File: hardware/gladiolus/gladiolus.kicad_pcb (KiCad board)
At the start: 4 copper layers, 70.7 x 53.3 mm, 94 parts, among them J1 NEIGHBOR1, J2 NEIGHBOR2, J7 BONUS_ROW, Q1 Q_NPN_BEC, U1 THS4520RGT, U2 AD8330ARQZ, U3 AD9283

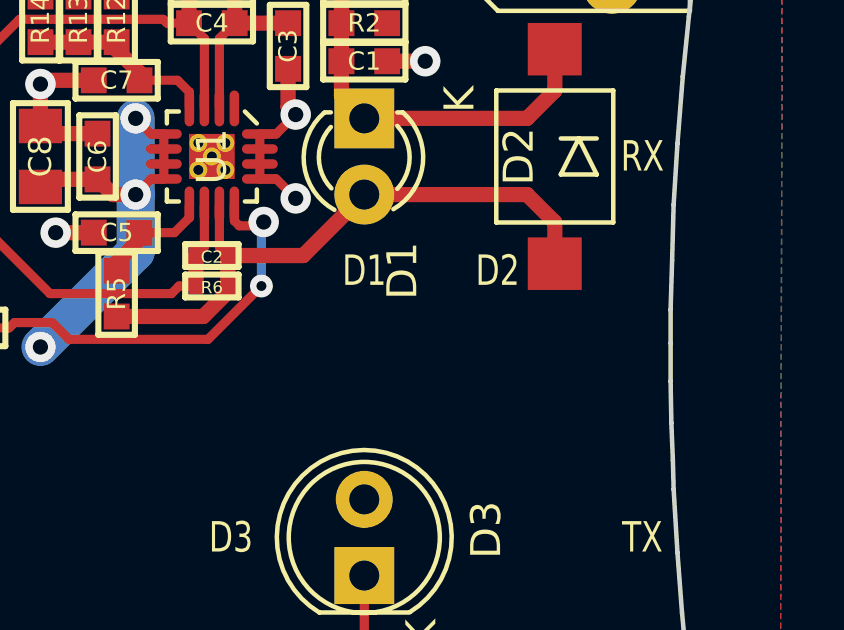
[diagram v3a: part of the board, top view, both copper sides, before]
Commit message: Gladiolus: added female header to block direct TX to RX light
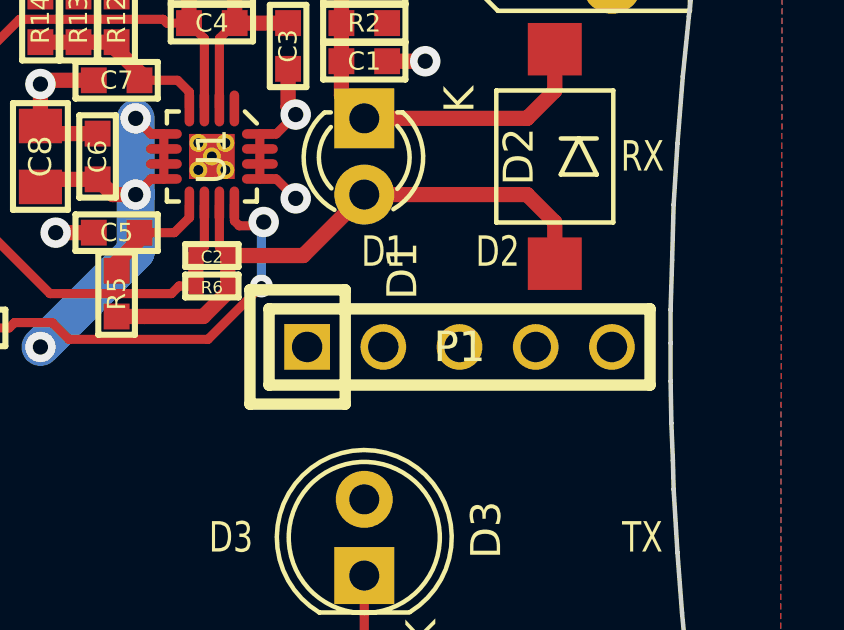
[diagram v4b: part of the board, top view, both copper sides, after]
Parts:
- added P1: CONN_01X05, gsg-modules:HEADER-1x5, F.Cu at (170.8, 95.2)
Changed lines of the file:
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@@
 (kicad_pcb (version 4) (host pcbnew 4.0.4-stable)
   (general
-    (links 228)
+    (links 233)
     (no_connects 0)
     (area 109.525999 68.504999 180.415001 121.995001)
@@
     (tracks 538)
     (zones 0)
-    (modules 94)
+    (modules 95)
     (nets 143)
   )
@@
       (net 132 "Net-(R33-Pad2)"))
   )
+  (module gsg-modules:HEADER-1x5 (layer F.Cu)
+    (at 170.815 95.25)
+    (tags CONN)
+    (fp_text reference P1 (at 0 0) (layer F.SilkS)
+      (effects (font (size 1.016 1.016) (thickness 0.2032)))
+    )
+    (fp_text value CONN_01X05 (at 0 0) (layer F.SilkS) hide
+      (effects (font (size 1.016 1.016) (thickness 0.2032)))
+    )
+    (fp_line (start -6.35 -1.27) (end 6.35 -1.27) (layer F.SilkS) (width 0.381))
+    (fp_line (start 6.35 -1.27) (end 6.35 1.27) (layer F.SilkS) (width 0.381))
+    (fp_line (start 6.35 1.27) (end -6.35 1.27) (layer F.SilkS) (width 0.381))
+    (fp_line (start -3.81 1.905) (end -3.81 -1.905) (layer F.SilkS) (width 0.381))
+    (fp_line (start -3.81 -1.905) (end -6.985 -1.905) (layer F.SilkS) (width 0.381))
+    (fp_line (start -6.985 -1.905) (end -6.985 1.905) (layer F.SilkS) (width 0.381))
+    (fp_line (start -6.35 -1.27) (end -6.35 1.27) (layer F.SilkS) (width 0.381))
+    (fp_line (start -6.985 1.905) (end -3.81 1.905) (layer F.SilkS) (width 0.381))
+    (pad 1 thru_hole rect (at -5.08 0) (size 1.524 1.524) (drill 1.016) (layers *.Cu *.Mask F.SilkS)
+      (net 1 GND))
+    (pad 2 thru_hole circle (at -2.54 0) (size 1.524 1.524) (drill 1.016) (layers *.Cu *.Mask F.SilkS)
+      (net 1 GND))
+    (pad 3 thru_hole circle (at 0 0) (size 1.524 1.524) (drill 1.016) (layers *.Cu *.Mask F.SilkS)
+      (net 1 GND))
+    (pad 4 thru_hole circle (at 2.54 0) (size 1.524 1.524) (drill 1.016) (layers *.Cu *.Mask F.SilkS)
+      (net 1 GND))
+    (pad 5 thru_hole circle (at 5.08 0) (size 1.524 1.524) (drill 1.016) (layers *.Cu *.Mask F.SilkS)
+      (net 1 GND))
+  )
   (gr_text TX (at 176.911 101.6) (layer F.SilkS)
     (effects (font (size 1.016 0.762) (thickness 0.1524)))
@@
     (effects (font (size 1.016 0.762) (thickness 0.1524)))
   )
-  (gr_text D2 (at 172.085 92.71) (layer F.SilkS)
+  (gr_text D2 (at 172.085 92.075) (layer F.SilkS)
     (effects (font (size 1.016 0.762) (thickness 0.1524)))
   )
-  (gr_text D1 (at 167.64 92.71) (layer F.SilkS)
+  (gr_text D1 (at 168.275 92.075) (layer F.SilkS)
     (effects (font (size 1.016 0.762) (thickness 0.1524)))
   )

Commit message: Gladiolus: length matching
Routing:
- net Net-(C2-Pad1): track 12.8 -> 13.3 mm
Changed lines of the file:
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@@
     (links 233)
     (no_connects 0)
-    (area 109.525999 68.504999 180.415001 121.995001)
+    (area 107.95 66.04 279.525801 124.460001)
     (thickness 1.6)
     (drawings 130)
@@
     (visible_elements FFFCFF7F)
     (pcbplotparams
-      (layerselection 0x010a8_80000007)
+      (layerselection 0x010a8_80000001)
       (usegerberextensions true)
       (excludeedgelayer true)
@@
   (segment (start 173.068 90.17) (end 173.99 91.092) (width 0.508) (layer F.Cu) (net 5))
   (segment (start 173.99 91.092) (end 173.99 92.475) (width 0.508) (layer F.Cu) (net 5))
-  (segment (start 154.9654 91.272362) (end 157.165038 93.472) (width 0.3048) (layer F.Cu) (net 6))
+  (segment (start 154.9654 92.186762) (end 156.250638 93.472) (width 0.3048) (layer F.Cu) (net 6))
   (segment (start 161.4678 93.218) (end 162.0266 93.218) (width 0.3048) (layer F.Cu) (net 6))
   (segment (start 161.2138 93.472) (end 161.4678 93.218) (width 0.3048) (layer F.Cu) (net 6))
-  (segment (start 157.165038 93.472) (end 161.2138 93.472) (width 0.3048) (layer F.Cu) (net 6))
-  (segment (start 154.9654 89.408) (end 154.9654 91.272362) (width 0.3048) (layer F.Cu) (net 6))
+  (segment (start 156.250638 93.472) (end 161.2138 93.472) (width 0.3048) (layer F.Cu) (net 6))
+  (segment (start 154.9654 89.408) (end 154.9654 92.186762) (width 0.3048) (layer F.Cu) (net 6))
   (segment (start 162.31 90.5) (end 162.31 91.9186) (width 0.3048) (layer F.Cu) (net 6))
   (segment (start 162.31 91.9186) (end 162.0266 92.202) (width 0.3048) (layer F.Cu) (net 6))

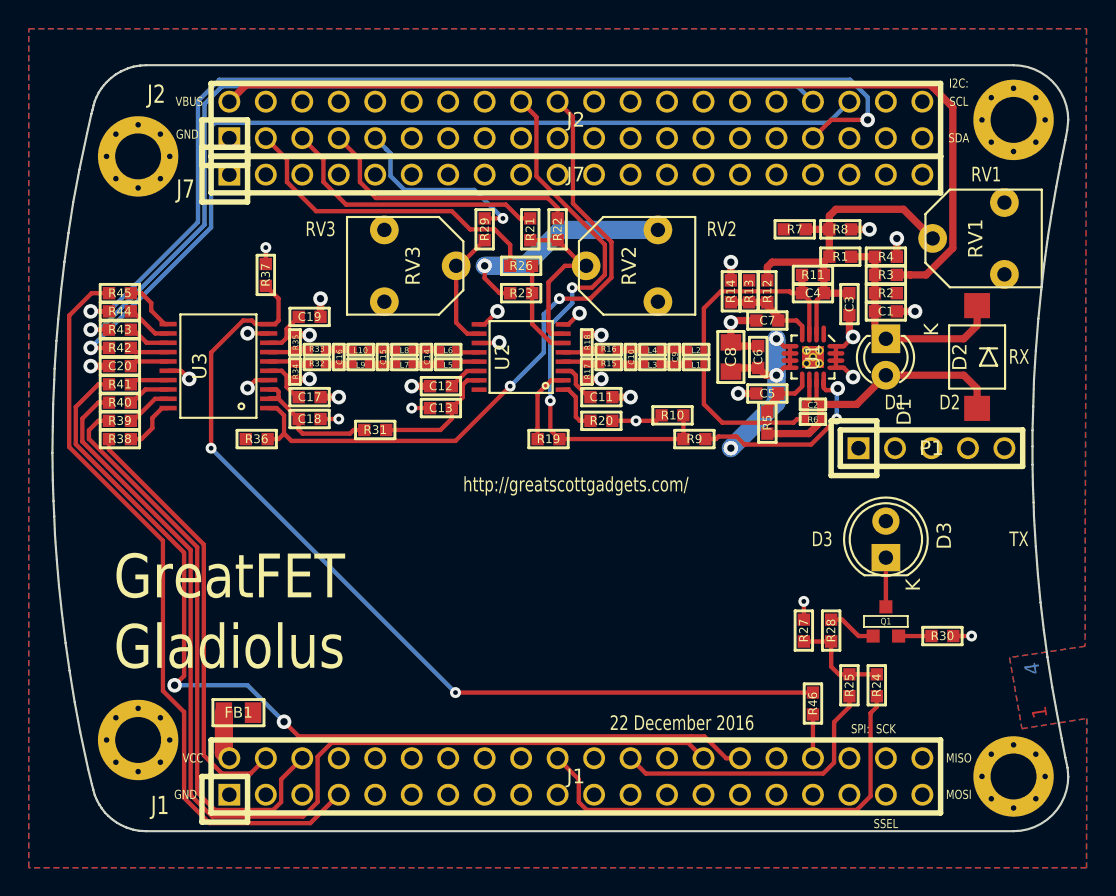
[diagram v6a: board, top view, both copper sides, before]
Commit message: Gladiolus: added TX DAC, changed TX GPIO pins
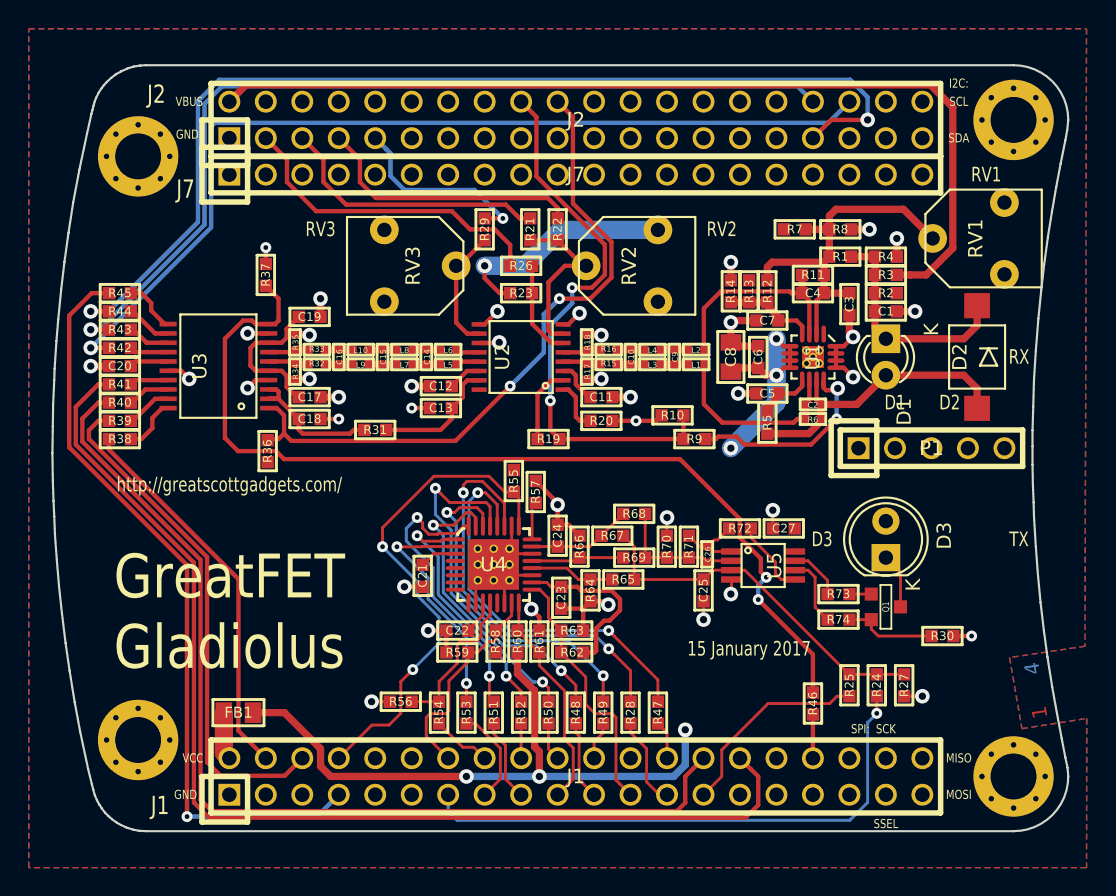
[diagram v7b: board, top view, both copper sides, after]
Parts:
- added C21: 100nF, gsg-modules:0603, F.Cu at (135.4, 104.1)
- added C22: 100nF, gsg-modules:0603, F.Cu at (137.8, 108.0)
- added C23: 100nF, gsg-modules:0603, F.Cu at (145.0, 105.7)
- added C24: 100nF, gsg-modules:0603, F.Cu at (144.8, 101.3)
- added C25: 100nF, gsg-modules:0603, F.Cu at (154.9, 105.2)
- added C26: 15pF, gsg-modules:0402, F.Cu at (155.2, 102.6)
- added C27: 100nF, gsg-modules:0603, F.Cu at (160.5, 100.8)
- added R47: 39, gsg-modules:0603, F.Cu at (151.8, 113.7)
- added R48: 39, gsg-modules:0603, F.Cu at (146.1, 113.7)
- added R49: 39, gsg-modules:0603, F.Cu at (148.0, 113.7)
- added R50: 39, gsg-modules:0603, F.Cu at (144.1, 113.7)
- added R51: 39, gsg-modules:0603, F.Cu at (140.3, 113.7)
- added R52: 39, gsg-modules:0603, F.Cu at (142.2, 113.7)
- added R53: 39, gsg-modules:0603, F.Cu at (138.4, 113.7)
- added R54: 39, gsg-modules:0603, F.Cu at (136.5, 113.7)
- added R55: 10k, gsg-modules:0603, F.Cu at (141.7, 97.5)
- added R56: R, gsg-modules:0603, F.Cu at (133.9, 112.9)
- added R57: 2k, gsg-modules:0603, F.Cu at (143.3, 98.3)
- added R58: 10k, gsg-modules:0603, F.Cu at (140.5, 108.7)
- added R59: 10k, gsg-modules:0603, F.Cu at (137.8, 109.5)
- added R60: 10k, gsg-modules:0603, F.Cu at (142.0, 108.7)
- added R61: 10k, gsg-modules:0603, F.Cu at (143.5, 108.7)
- added R62: 10k, gsg-modules:0603, F.Cu at (145.8, 109.5)
- added R63: 10k, gsg-modules:0603, F.Cu at (145.8, 108.0)
- added R64: 250, gsg-modules:0603, F.Cu at (147.1, 105.2)
- added R65: R, gsg-modules:0603, F.Cu at (149.4, 104.4)
- added R66: 250, gsg-modules:0603, F.Cu at (146.3, 102.1)
- added R67: 0, gsg-modules:0603, F.Cu at (148.6, 101.3)
- added R68: R, gsg-modules:0603, F.Cu at (150.1, 99.8)
- added R69: 250, gsg-modules:0603, F.Cu at (150.1, 102.9)
- added R70: 953, gsg-modules:0603, F.Cu at (152.4, 102.1)
- added R71: 1000, gsg-modules:0603, F.Cu at (153.9, 102.1)
- added R72: 0, gsg-modules:0603, F.Cu at (157.5, 100.8)
- added R73: 1k, gsg-modules:0603, F.Cu at (164.3, 105.4)
- added R74: 0, gsg-modules:0603, F.Cu at (164.3, 107.2)
- added U4: AD9704, gsg-modules:QFN32-5, F.Cu at (140.3, 103.3)
- added U5: LMH6643, gsg-modules:VSSOP8, F.Cu at (159.1, 103.4)
- R24, R25: value 0 -> 1k
- R28: value 1k -> 39
- moved R28 15.1 mm to (149.9, 113.7)
- moved R27 7.96 mm to (168.9, 111.8)
- moved R36 1.13 mm to (124.6, 95.5), turned to 270 degrees
- moved Q1 1.02 mm to (167.6, 106.3), turned to 90 degrees
- turned R24 to 270 degrees
- turned R25 to 270 degrees
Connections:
- R24 pad 1: /P1_10 -> Net-(C25-Pad1)
- R24 pad 2: Net-(R24-Pad2) -> /P1_5
- R25 pad 1: /P5_4 -> Net-(C25-Pad1)
- R25 pad 2: Net-(R24-Pad2) -> /P5_6
- R27 pad 1: GND -> Net-(C25-Pad1)
- R27 pad 2: Net-(R24-Pad2) -> GND
- R28 pad 1: Net-(Q1-Pad1) -> Net-(R28-Pad1)
- R28 pad 2: Net-(R24-Pad2) -> /P1_14
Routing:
- net VCC: track 47.0 -> 112.8 mm, vias 4 -> 7
- net /P1_5: track 0.00 -> 38.8 mm, vias 0 -> 1
- net /P5_0: track 0.00 -> 34.9 mm, vias 0 -> 2
- net GND: track 47.3 -> 78.3 mm, vias 29 -> 39
- net /P1_10: track 31.8 -> 2.68 mm
- net Net-(R28-Pad1): track 0.00 -> 28.7 mm, vias 0 -> 2
- net Net-(R47-Pad1): track 0.00 -> 27.5 mm, vias 0 -> 2
- net Net-(R48-Pad1): track 0.00 -> 25.9 mm, vias 0 -> 2
- net Net-(C25-Pad1): track 0.00 -> 25.4 mm
- net Net-(R49-Pad1): track 0.00 -> 23.9 mm, vias 0 -> 2
- net Net-(R51-Pad1): track 0.00 -> 20.2 mm, vias 0 -> 2
- net Net-(R50-Pad1): track 0.00 -> 20.1 mm, vias 0 -> 2
- net /P5_4: track 20.0 -> 0.00 mm
- net /P5_5: track 0.00 -> 18.1 mm
- net Net-(R52-Pad1): track 0.00 -> 17.4 mm, vias 0 -> 2
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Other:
- board text added: "15 January 2017"
- board text removed: "22 December 2016"

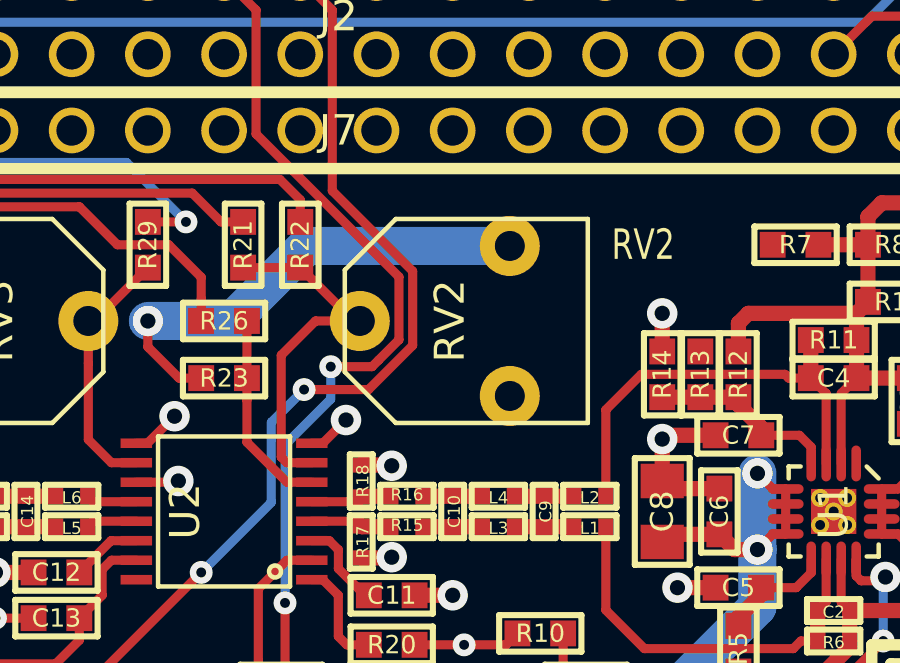
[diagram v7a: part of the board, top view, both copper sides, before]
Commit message: Gladiolus: corrected voltage range of RV2
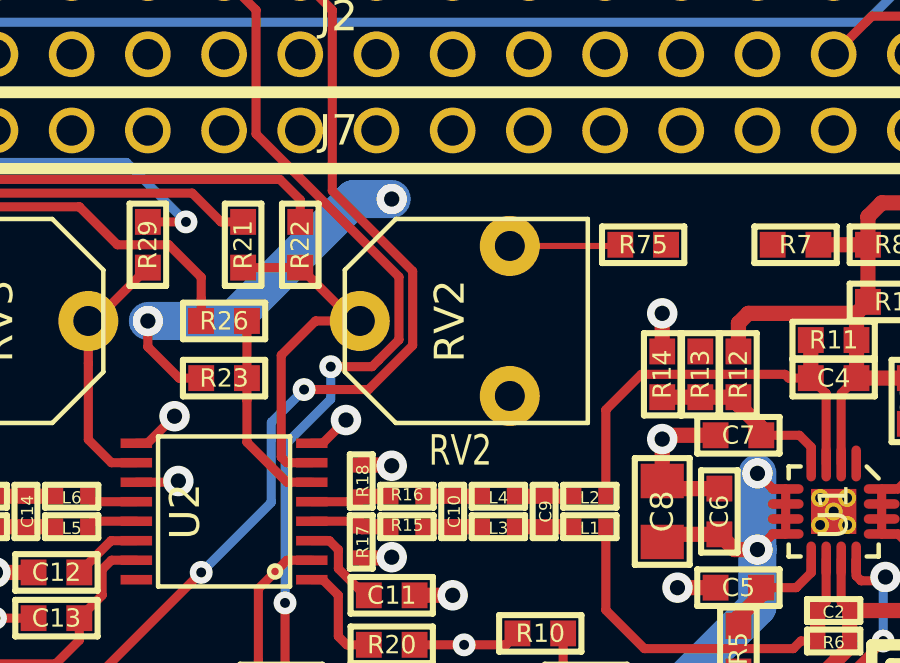
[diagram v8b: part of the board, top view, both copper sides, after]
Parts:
- added R75: 12k, gsg-modules:0603, F.Cu at (156.2, 80.0)
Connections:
- RV2 pad 3: VCC -> Net-(R75-Pad1)
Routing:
- net Net-(R75-Pad1): track 0.00 -> 3.70 mm
- net VCC: track 112.8 -> 109.5 mm, vias 7 -> 8
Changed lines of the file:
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@@
 (kicad_pcb (version 4) (host pcbnew 4.0.4-stable)
   (general
-    (links 337)
+    (links 338)
     (no_connects 0)
     (area 109.525999 68.504999 180.415001 121.995001)
     (thickness 1.6)
     (drawings 130)
-    (tracks 893)
+    (tracks 896)
     (zones 0)
-    (modules 132)
-    (nets 168)
+    (modules 133)
+    (nets 169)
   )
   (page A4)
@@
   )
   (setup
-    (last_trace_width 0.3048)
+    (last_trace_width 1.27)
     (user_trace_width 0.3048)
     (user_trace_width 0.508)
@@
   (net 166 "Net-(U4-Pad9)")
   (net 167 "Net-(U4-Pad13)")
+  (net 168 "Net-(R75-Pad1)")
   (net_class Default "This is the default net class."
     (clearance 0.1524)
@@
     (add_net "Net-(R73-Pad2)")
     (add_net "Net-(R74-Pad1)")
+    (add_net "Net-(R75-Pad1)")
     (add_net "Net-(R9-Pad1)")
     (add_net "Net-(U1-Pad1)")
@@
       (net 127 "Net-(R21-Pad1)"))
     (pad 3 thru_hole circle (at 2.5 0 90) (size 2 2) (drill 1) (layers *.Cu *.Mask)
-      (net 2 VCC))
+      (net 168 "Net-(R75-Pad1)"))
   )
   (module gsg-modules:3306F (layer F.Cu)
@@
       (net 145 "Net-(C26-Pad1)"))
   )
+  (module gsg-modules:0603 (layer F.Cu)
+    (at 156.21 80.01)
+    (fp_text reference R75 (at 0 0) (layer F.SilkS)
+      (effects (font (size 0.6096 0.6096) (thickness 0.1524)))
+    )
+    (fp_text value 12k (at 0 0) (layer F.SilkS) hide
+      (effects (font (size 0.6096 0.6096) (thickness 0.1524)))
+    )
+    (fp_line (start 1.3716 -0.6096) (end -1.3716 -0.6096) (layer F.SilkS) (width 0.2032))
+    (fp_line (start -1.3716 -0.6096) (end -1.3716 0.6096) (layer F.SilkS) (width 0.2032))
+    (fp_line (start -1.3716 0.6096) (end 1.3716 0.6096) (layer F.SilkS) (width 0.2032))
+    (fp_line (start 1.3716 0.6096) (end 1.3716 -0.6096) (layer F.SilkS) (width 0.2032))
+    (pad 2 smd rect (at 0.762 0) (size 0.8636 0.8636) (layers F.Cu F.Paste F.Mask)
+      (net 2 VCC))
+    (pad 1 smd rect (at -0.762 0) (size 0.8636 0.8636) (layers F.Cu F.Paste F.Mask)
+      (net 168 "Net-(R75-Pad1)"))
+  )
   (gr_text TX (at 176.911 101.6) (layer F.SilkS)
     (effects (font (size 1.016 0.762) (thickness 0.1524)))
@@
     (effects (font (size 1.016 0.762) (thickness 0.1524)))
   )
-  (gr_text RV2 (at 156.21 80.01) (layer F.SilkS)
+  (gr_text RV2 (at 150.114 86.868) (layer F.SilkS)
     (effects (font (size 1.016 0.762) (thickness 0.1524)))
   )
@@
   (segment (start 164.707 88.15) (end 165.354 87.503) (width 0.3048) (layer F.Cu) (net 1))
   (via (at 165.354 87.503) (size 1.016) (drill 0.508) (layers F.Cu B.Cu) (net 1))
+  (segment (start 142.494 82.55) (end 146.558 78.486) (width 1.27) (layer B.Cu) (net 2))
+  (segment (start 146.558 78.486) (end 147.828 78.486) (width 1.27) (layer B.Cu) (net 2))
+  (via (at 147.828 78.486) (size 1.016) (drill 0.508) (layers F.Cu B.Cu) (net 2))
   (segment (start 123.3932 88.27) (end 123.3932 89.5) (width 0.3048) (layer F.Cu) (net 2))
   (segment (start 123.3932 89.5) (end 123.7532 89.86) (width 0.3048) (layer F.Cu) (net 2))
@@
   (segment (start 143.002 104.6) (end 144.018045 104.6) (width 0.2032) (layer F.Cu) (net 2))
   (segment (start 144.018045 104.6) (end 144.309849 104.891804) (width 0.2032) (layer F.Cu) (net 2))
-  (segment (start 142.494 82.55) (end 144.994 80.05) (width 1.27) (layer B.Cu) (net 2))
-  (segment (start 144.994 80.05) (end 151.765 80.05) (width 1.27) (layer B.Cu) (net 2))
-  (segment (start 139.7 82.55) (end 142.494 82.55) (width 1.27) (layer B.Cu) (net 2))
   (segment (start 141.478 84.455) (end 140.7414 84.455) (width 0.3048) (layer F.Cu) (net 2))
   (segment (start 140.7414 84.455) (end 139.7 83.4136) (width 0.3048) (layer F.Cu) (net 2))
   (segment (start 139.7 83.4136) (end 139.7 82.55) (width 0.3048) (layer F.Cu) (net 2))
-  (via (at 139.7 82.55) (size 1.016) (drill 0.508) (layers F.Cu B.Cu) (net 2))
   (segment (start 124.658 89.86) (end 125.5628 89.86) (width 0.3048) (layer F.Cu) (net 2))
   (segment (start 125.5628 89.86) (end 125.907799 90.204999) (width 0.3048) (layer F.Cu) (net 2))
@@
   (segment (start 160.54 88.15) (end 160.02 87.63) (width 0.3048) (layer F.Cu) (net 2))
   (via (at 160.02 87.63) (size 1.016) (drill 0.508) (layers F.Cu B.Cu) (net 2))
+  (via (at 139.7 82.55) (size 1.016) (drill 0.508) (layers F.Cu B.Cu) (net 2))
+  (segment (start 139.7 82.55) (end 142.494 82.55) (width 1.27) (layer B.Cu) (net 2))
   (segment (start 121.92 71.12) (end 123.088401 69.951599) (width 0.508) (layer F.Cu) (net 3))
   (segment (start 123.088401 69.951599) (end 170.740833 69.951599) (width 0.508) (layer F.Cu) (net 3))
@@
   (segment (start 161.29 103.744) (end 162.2182 103.744) (width 0.2032) (layer F.Cu) (net 160))
   (segment (start 162.2182 103.744) (end 162.7124 104.2382) (width 0.2032) (layer F.Cu) (net 160))
+  (segment (start 151.765 80.05) (end 155.408 80.05) (width 0.2032) (layer F.Cu) (net 168))
+  (segment (start 155.408 80.05) (end 155.448 80.01) (width 0.2032) (layer F.Cu) (net 168))
   (zone (net 2) (net_name VCC) (layer F.Cu) (hatch edge 0.508)
     (connect_pads (clearance 0.254))
